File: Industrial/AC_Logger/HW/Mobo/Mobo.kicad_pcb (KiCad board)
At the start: 2 copper layers, 72.6 x 22.9 mm, 6 parts

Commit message: Started new PCB
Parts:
- added A1: Arduino_UNO_R3, For_Rasterboard:Arduino_UNO_R3_WithMountingHoles_Snapped_to_P2.54mm, B.Cu at (53.3, 40.6)
- added ControlPins1: Conn_01x09_Male, Connector_PinHeader_2.00mm:PinHeader_1x09_P2.00mm_Vertical, F.Cu at (236.5, 16.5)
- added Power1: Conn_01x03_Male, Connector_PinHeader_2.00mm:PinHeader_1x03_P2.00mm_Vertical, F.Cu at (160.0, 71.4)
- added RTC1: Conn_01x05_Female, Connector_PinSocket_2.00mm:PinSocket_1x05_P2.00mm_Vertical, F.Cu at (236.5, 50.6)
- added RTC2: Conn_01x05_Female, Connector_PinSocket_2.54mm:PinSocket_1x05_P2.54mm_Vertical, F.Cu at (114.3, 43.1)
- added microSD1: Conn_01x06_Female, Connector_PinSocket_2.00mm:PinSocket_1x06_P2.00mm_Vertical, F.Cu at (240.5, 16.5)
- added microSD2: Conn_01x06_Female, Connector_PinSocket_2.00mm:PinSocket_1x06_P2.00mm_Vertical, F.Cu at (236.5, 36.5)
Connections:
- R1 pad 1: Net-(J3-Pad4) -> Net-(ControlPins1-Pad2)
- R1 pad 2: Net-(J4-Pad1) -> Net-(Power1-Pad1)
- R2 pad 1: Net-(J2-Pad1) -> Net-(ControlPins1-Pad1)
- R2 pad 2: Net-(J4-Pad1) -> Net-(Power1-Pad1)
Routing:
- net +3V3: track 0.00 -> 111.8 mm, vias 0 -> 4
- net /SCL: track 0.00 -> 17.8 mm, vias 0 -> 2
- net /SDA: track 0.00 -> 12.7 mm
- net GND: track 0.00 -> 12.7 mm

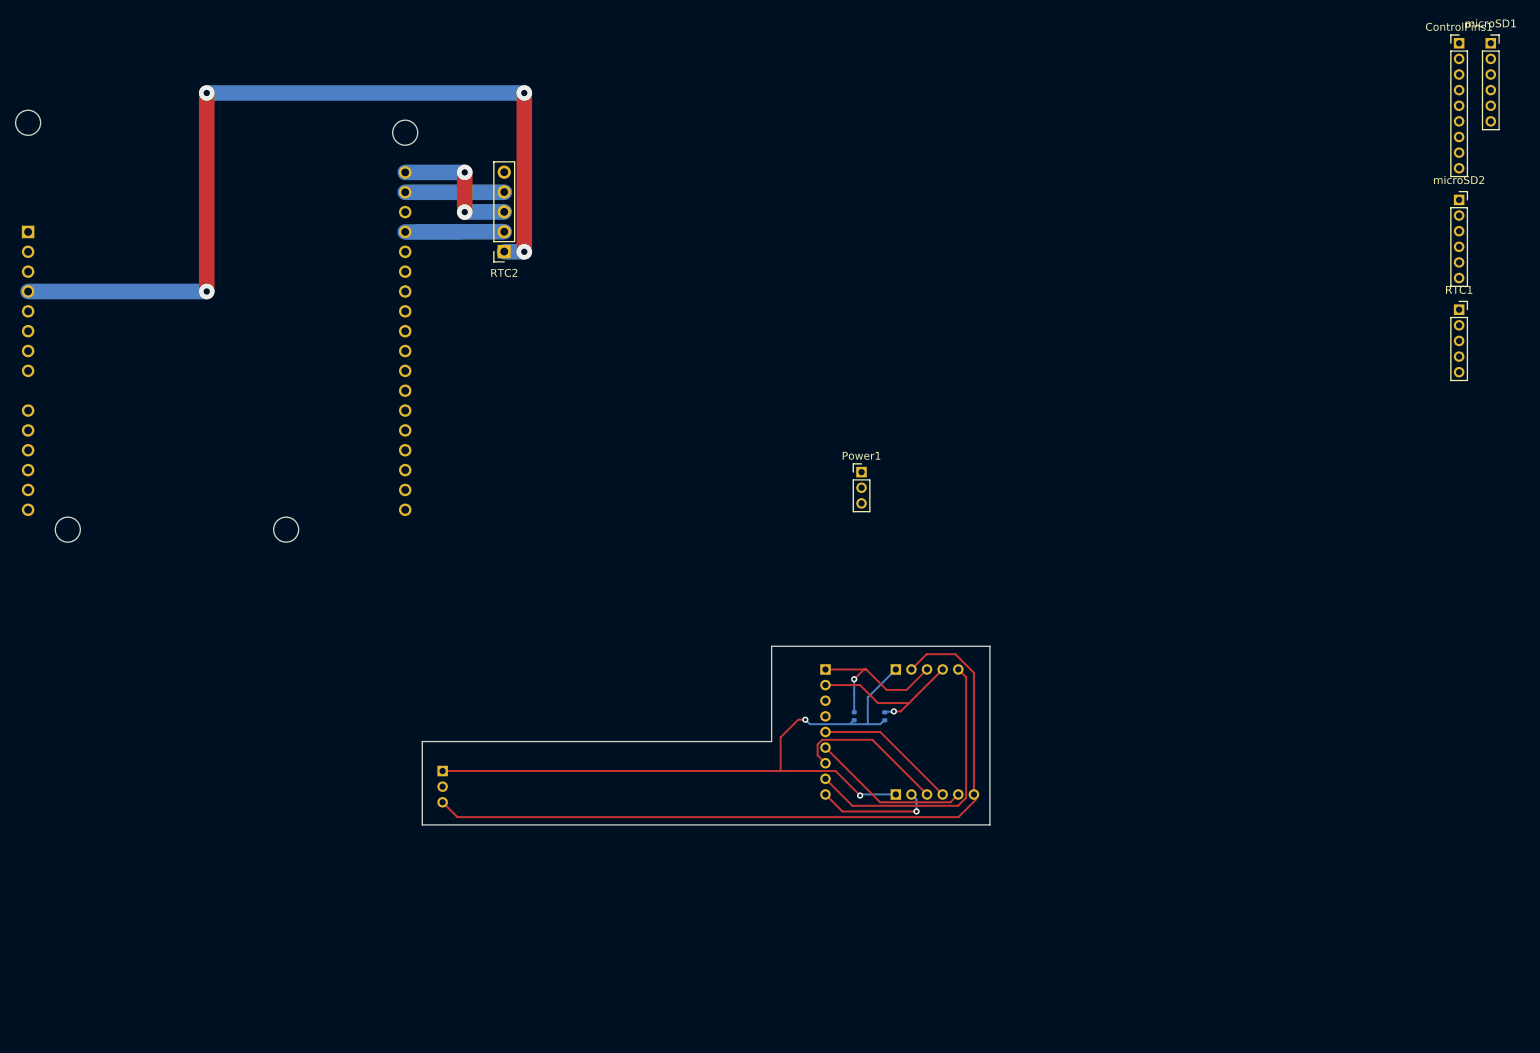
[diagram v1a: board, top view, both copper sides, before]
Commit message: Finished stripboard design
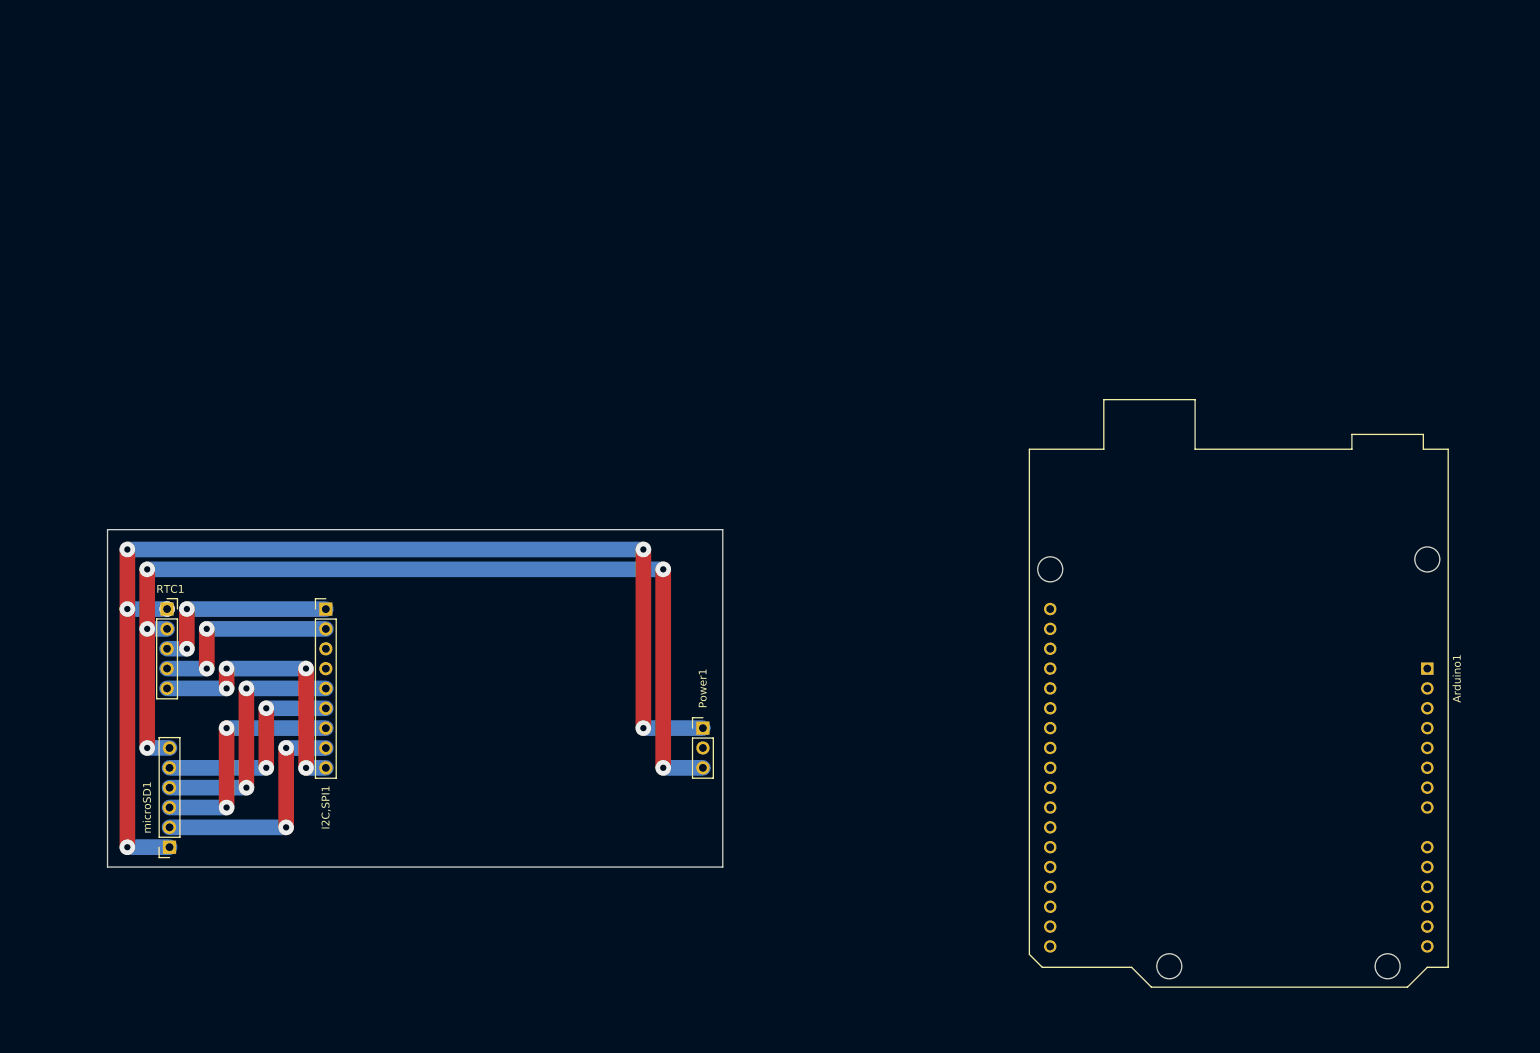
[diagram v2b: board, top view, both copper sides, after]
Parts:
- removed Control: Conn_01x09_Male, Connector_PinHeader_2.00mm:PinHeader_1x09_P2.00mm_Vertical
- removed Power: Conn_01x03_Male, Connector_PinHeader_2.00mm:PinHeader_1x03_P2.00mm_Vertical
- removed R1, R2: 4.7k, Resistor_SMD:R_0402_1005Metric
- removed RTC: Conn_01x05_Female, Connector_PinSocket_2.00mm:PinSocket_1x05_P2.00mm_Vertical
- removed the RTC1 at (236.5, 50.6)
- removed SD, microSD2: Conn_01x06_Female, Connector_PinSocket_2.00mm:PinSocket_1x06_P2.00mm_Vertical
- Arduino1: renamed from A1; value Arduino_UNO_R3 -> Arduino UNO R3; moved to F.Cu
- I2C,SPI1: renamed from ControlPins1; footprint Connector_PinHeader_2.00mm:PinHeader_1x09_P2.00mm_Vertical -> Connector_PinHeader_2.54mm:PinHeader_1x09_P2.54mm_Vertical
- Power1: footprint Connector_PinHeader_2.00mm:PinHeader_1x03_P2.00mm_Vertical -> Connector_PinHeader_2.54mm:PinHeader_1x03_P2.54mm_Vertical
- microSD1: footprint Connector_PinSocket_2.00mm:PinSocket_1x06_P2.00mm_Vertical -> Connector_PinSocket_2.54mm:PinSocket_1x06_P2.54mm_Vertical
- moved microSD1 197.9 mm to (71.4, 119.4), turned to 180 degrees
- moved Arduino1 187.6 mm to (232.4, 96.5)
- moved I2C,SPI1 162.1 mm to (91.4, 88.9)
- moved RTC1 62.9 mm to (71.1, 88.9), turned to 0 degrees
- moved Power1 38.5 mm to (139.7, 104.1)
- renumbered RTC2 to RTC1
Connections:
- Arduino1 pad 24: unconnected-(A1-Pad24) -> /RTC RST
- Arduino1 pad 25: unconnected-(A1-Pad25) -> /SS
- Arduino1 pad 26: unconnected-(A1-Pad26) -> /MOSI
- Arduino1 pad 27: unconnected-(A1-Pad27) -> /MISO
- Arduino1 pad 28: unconnected-(A1-Pad28) -> /SCK
- Arduino1 pad 29: GND -> unconnected-(Arduino1-Pad29)
- Arduino1 pad 4: +3V3 -> /3V3
- Arduino1 pad 5: unconnected-(A1-Pad5) -> /5V
- Arduino1 pad 6: unconnected-(A1-Pad6) -> /GND
- I2C,SPI1 pad 1: Net-(ControlPins1-Pad1) -> /SCL
- I2C,SPI1 pad 2: Net-(ControlPins1-Pad2) -> /SDA
- I2C,SPI1 pad 5: Net-(ControlPins1-Pad5) -> /SCK
- I2C,SPI1 pad 6: Net-(ControlPins1-Pad6) -> /MISO
- I2C,SPI1 pad 7: Net-(ControlPins1-Pad7) -> /MOSI
- I2C,SPI1 pad 8: Net-(ControlPins1-Pad8) -> /SS
- I2C,SPI1 pad 9: Net-(ControlPins1-Pad9) -> /RTC RST
- Power1 pad 1: Net-(Power1-Pad1) -> /3V3
- Power1 pad 2: unconnected-(Power1-Pad2) -> /5V
- Power1 pad 3: Net-(Power1-Pad3) -> /GND
- RTC1 pad 1: +3V3 -> /3V3
- RTC1 pad 2: GND -> /GND
- RTC1 pad 5: unconnected-(RTC2-Pad5) -> /RTC RST
- microSD1 pad 1: Net-(Power1-Pad1) -> /3V3
- microSD1 pad 2: Net-(ControlPins1-Pad9) -> /SS
- microSD1 pad 3: Net-(ControlPins1-Pad7) -> /MOSI
- microSD1 pad 4: Net-(ControlPins1-Pad5) -> /SCK
- microSD1 pad 5: Net-(ControlPins1-Pad6) -> /MISO
- microSD1 pad 6: Net-(Power1-Pad3) -> /GND
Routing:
- net /3V3: track 0.00 -> 145.1 mm, vias 0 -> 6
- net /GND: track 0.00 -> 124.8 mm, vias 0 -> 5
- net +3V3: track 111.8 -> 0.00 mm, vias 4 -> 0
- net Net-(J1-Pad3): track 95.4 -> 0.00 mm
- net Net-(J4-Pad1): track 87.7 -> 0.00 mm, vias 2 -> 0
- net Net-(J2-Pad8): track 36.7 -> 0.00 mm
- net /RTC RST: track 0.00 -> 35.6 mm, vias 0 -> 4
- net /SCK: track 0.00 -> 32.7 mm, vias 0 -> 2
- net /SS: track 0.00 -> 30.2 mm, vias 0 -> 2
- net /MOSI: track 0.00 -> 30.2 mm, vias 0 -> 2
- net /MISO: track 0.00 -> 27.6 mm, vias 0 -> 2
- net Net-(J2-Pad1): track 21.4 -> 0.00 mm, vias 1 -> 0
- net Net-(J3-Pad4): track 21.3 -> 0.00 mm, vias 1 -> 0
- net Net-(J2-Pad6): track 20.3 -> 0.00 mm
- net Net-(J2-Pad7): track 20.0 -> 0.00 mm
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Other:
- board size 72.6 x 22.9 mm -> 78.7 x 43.2 mm
- board text removed: "3.3V"
- board text removed: "SCL"

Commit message: Last last edit to pcb
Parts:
- removed I2C,SPI1: Conn_01x09_Male, Connector_PinHeader_2.54mm:PinHeader_1x09_P2.54mm_Vertical
- removed Power1: Conn_01x03_Male, Connector_PinHeader_2.54mm:PinHeader_1x03_P2.54mm_Vertical
- added J1: Conn_01x11_Female, Connector_PinSocket_2.54mm:PinSocket_1x11_P2.54mm_Vertical, B.Cu at (114.3, 94.0)
- moved Arduino1 115.8 mm to (116.8, 104.1), turned to 90 degrees
- moved microSD1 112.4 mm to (180.3, 91.4), turned to 0 degrees
- moved RTC1 110.0 mm to (175.3, 124.5), turned to 180 degrees
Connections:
- Arduino1 pad 10: unconnected-(Arduino1-Pad10) -> /A1
- Arduino1 pad 11: unconnected-(Arduino1-Pad11) -> /A2
- Arduino1 pad 12: unconnected-(Arduino1-Pad12) -> /A3
- Arduino1 pad 13: unconnected-(Arduino1-Pad13) -> /A4
- Arduino1 pad 14: unconnected-(Arduino1-Pad14) -> /A5
- Arduino1 pad 23: unconnected-(Arduino1-Pad23) -> /RTC RST
- Arduino1 pad 24: /RTC RST -> unconnected-(Arduino1-Pad24)
- Arduino1 pad 29: unconnected-(Arduino1-Pad29) -> GND
- Arduino1 pad 4: /3V3 -> unconnected-(Arduino1-Pad4)
- Arduino1 pad 5: /5V -> +5V
- Arduino1 pad 6: /GND -> GND
- Arduino1 pad 7: unconnected-(Arduino1-Pad7) -> GND
- Arduino1 pad 8: unconnected-(Arduino1-Pad8) -> /VIN
- Arduino1 pad 9: unconnected-(Arduino1-Pad9) -> /A0
- RTC1 pad 1: /3V3 -> +5V
- RTC1 pad 2: /GND -> GND
- microSD1 pad 1: /3V3 -> +5V
- microSD1 pad 6: /GND -> GND
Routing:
- net /3V3: track 145.1 -> 0.00 mm, vias 6 -> 0
- net +5V: track 0.00 -> 132.1 mm, vias 0 -> 4
- net /GND: track 124.8 -> 0.00 mm, vias 5 -> 0
- net GND: track 0.00 -> 35.6 mm, vias 0 -> 2
- net /RTC RST: track 35.6 -> 55.9 mm, vias 4 -> 2
- net /SS: track 30.2 -> 15.2 mm, vias 2 -> 0
- net /SCK: track 32.7 -> 17.8 mm, vias 2 -> 0
- net /MOSI: track 30.2 -> 15.2 mm, vias 2 -> 0
- net /MISO: track 27.6 -> 16.3 mm
- net /SCL: track 25.4 -> 17.8 mm
- net /VIN: track 0.00 -> 2.54 mm
- net /A5: track 0.00 -> 2.54 mm
- net /A4: track 0.00 -> 2.54 mm
- net /A3: track 0.00 -> 2.54 mm
- net /A2: track 0.00 -> 2.54 mm
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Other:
- board size 78.7 x 43.2 mm -> 76.2 x 61 mm

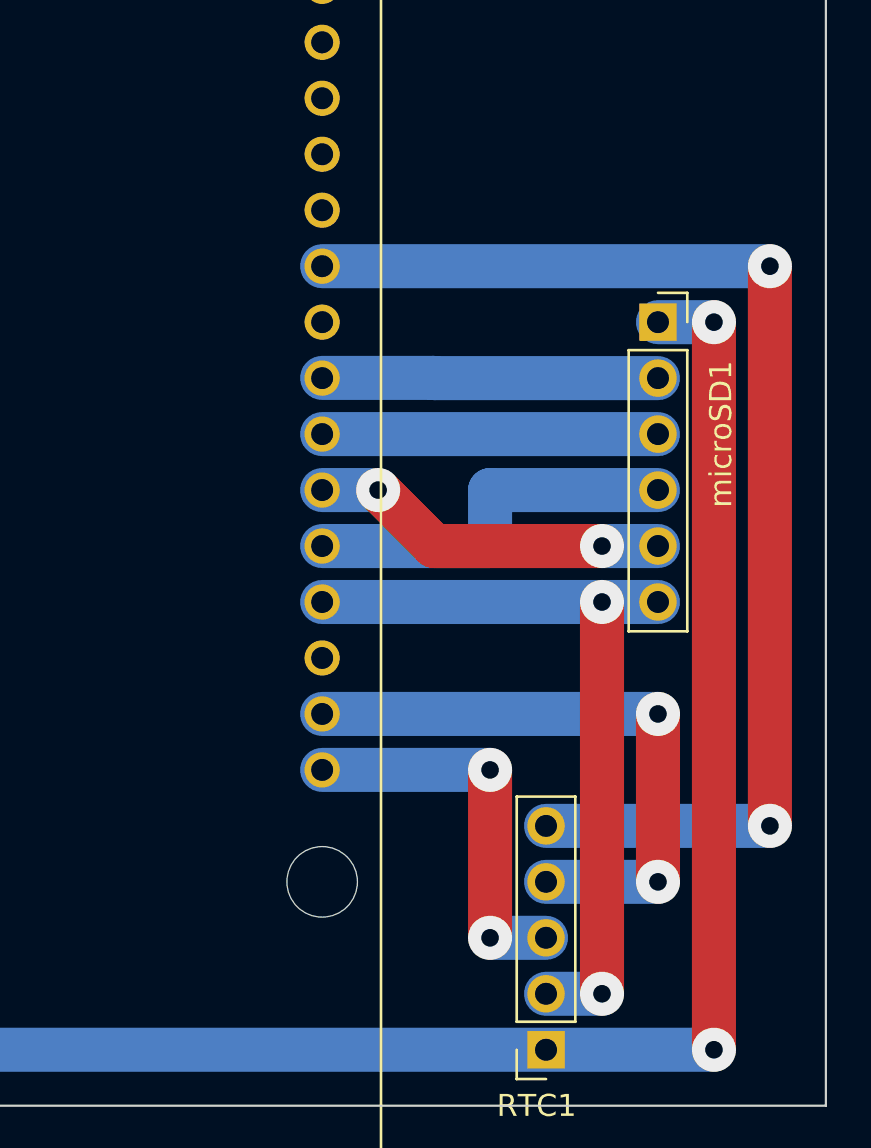
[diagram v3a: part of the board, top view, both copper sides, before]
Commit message: PCB final, instructions for handling SD module
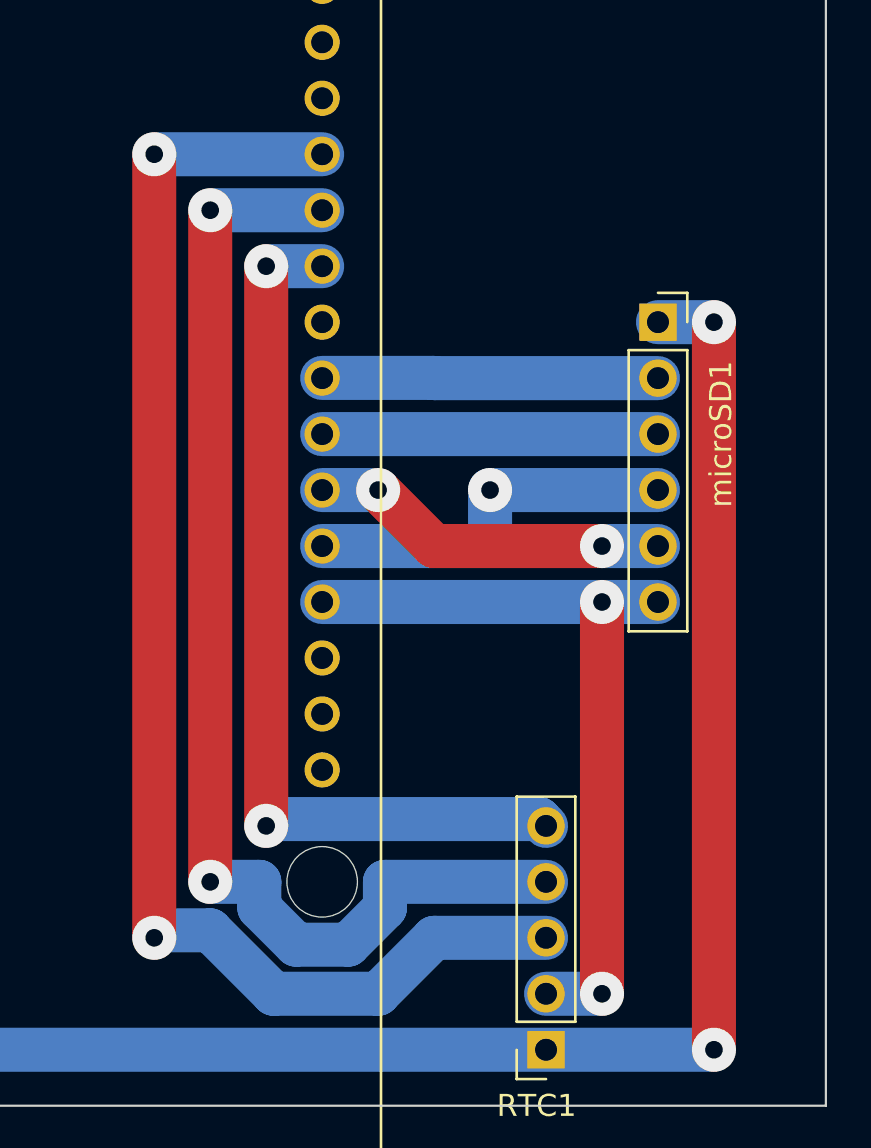
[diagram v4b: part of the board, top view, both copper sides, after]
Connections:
- net /RTC RST renamed /D23
- Arduino1 pad 21: unconnected-(Arduino1-Pad21) -> /D21
- Arduino1 pad 22: unconnected-(Arduino1-Pad22) -> /D22
- Arduino1 pad 31: /SDA -> unconnected-(Arduino1-Pad31)
- Arduino1 pad 32: /SCL -> unconnected-(Arduino1-Pad32)
- RTC1 pad 3: /SCL -> /D21
- RTC1 pad 4: /SDA -> /D22
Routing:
- net /D21: track 0.00 -> 63.2 mm, vias 0 -> 2
- net /D22: track 0.00 -> 54.5 mm, vias 0 -> 2
- net /SDA: track 27.9 -> 0.00 mm, vias 2 -> 0
- net /SCL: track 17.8 -> 0.00 mm, vias 2 -> 0
- net /D23: track 55.9 -> 40.9 mm
- net /SCK: vias 0 -> 1

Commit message: Finising touches on PCB and Schematic
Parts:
- added R1: 4K7, Resistor_THT:R_Axial_DIN0207_L6.3mm_D2.5mm_P7.62mm_Horizontal, F.Cu at (132.3, 121.9)
- added R2: 4K7, Resistor_THT:R_Axial_DIN0207_L6.3mm_D2.5mm_P7.62mm_Horizontal, F.Cu at (128.3, 121.9)
- moved Arduino1 5.24 mm to (115.6, 109.2)
- moved microSD1 5.24 mm to (179.1, 96.5)
- moved V_Sensors_Header1 5.24 mm to (113.0, 99.1)
- moved RTC1 5.24 mm to (174.0, 129.5)
- renumbered J1 to V_Sensors_Header1
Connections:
- net /A0 renamed Net-(Arduino1-Pad9)
- net /A1 renamed Net-(Arduino1-Pad10)
- net /A2 renamed Net-(Arduino1-Pad11)
- net /A3 renamed Net-(Arduino1-Pad12)
- net /A4 renamed Net-(Arduino1-Pad13)
- net /A5 renamed Net-(Arduino1-Pad14)
- Arduino1 pad 29: GND -> GND1
- Arduino1 pad 7: GND -> unconnected-(Arduino1-Pad7)
- RTC1 pad 2: GND -> GND1
- microSD1 pad 6: GND -> GND1
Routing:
- net /D22: track 54.5 -> 90.1 mm, vias 2 -> 5
- net GND: track 35.6 -> 0.00 mm, vias 2 -> 0
- net GND1: track 0.00 -> 35.6 mm, vias 0 -> 2
- net /D21: track 63.2 -> 89.6 mm, vias 2 -> 4
- net +5V: track 132.1 -> 134.6 mm
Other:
- board size 76.2 x 61 mm -> 73.7 x 66 mm
